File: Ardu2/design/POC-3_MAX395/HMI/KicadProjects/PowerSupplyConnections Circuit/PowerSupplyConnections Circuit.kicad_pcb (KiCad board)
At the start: 2 copper layers, 51.1 x 42.9 mm, 20 parts, among them P1 GND, P2 GND, P3 Wiper, P4 Wiper, P5 3.3v, P6 5v

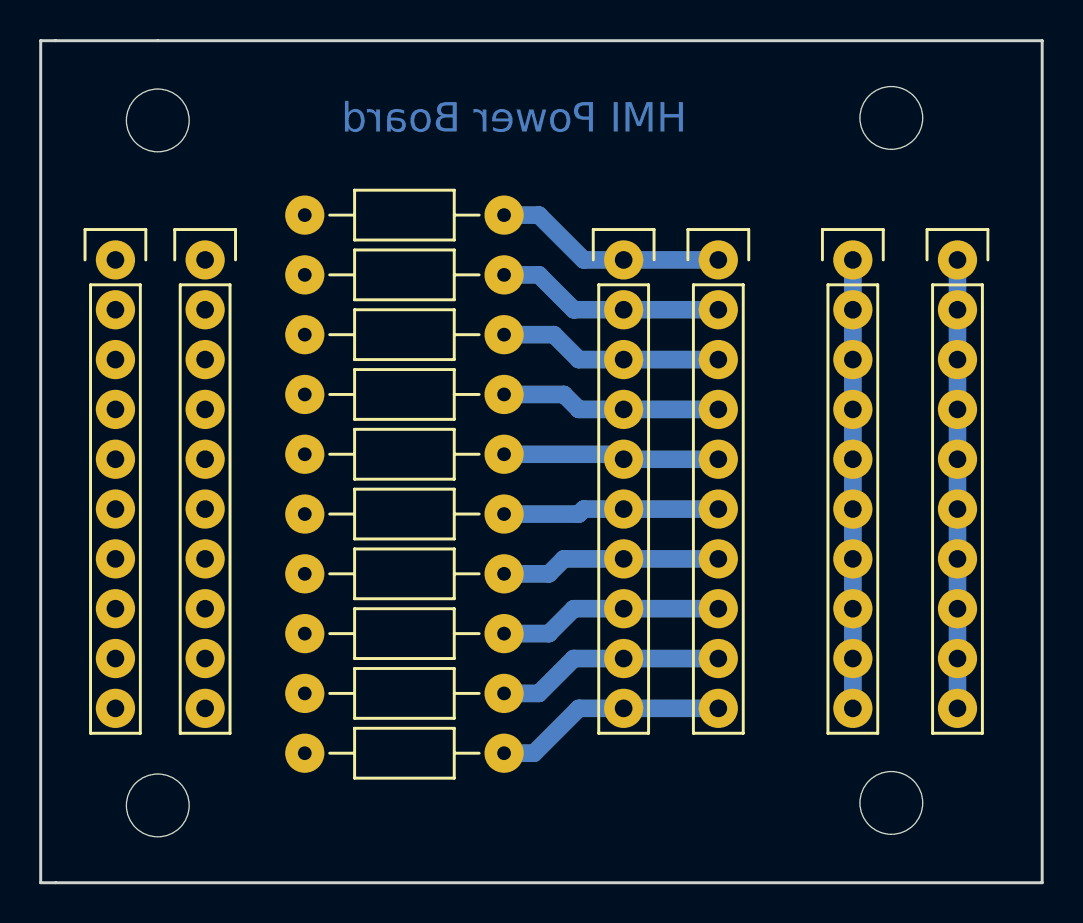
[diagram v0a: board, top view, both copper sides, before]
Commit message: final version pf power distribution board pcb
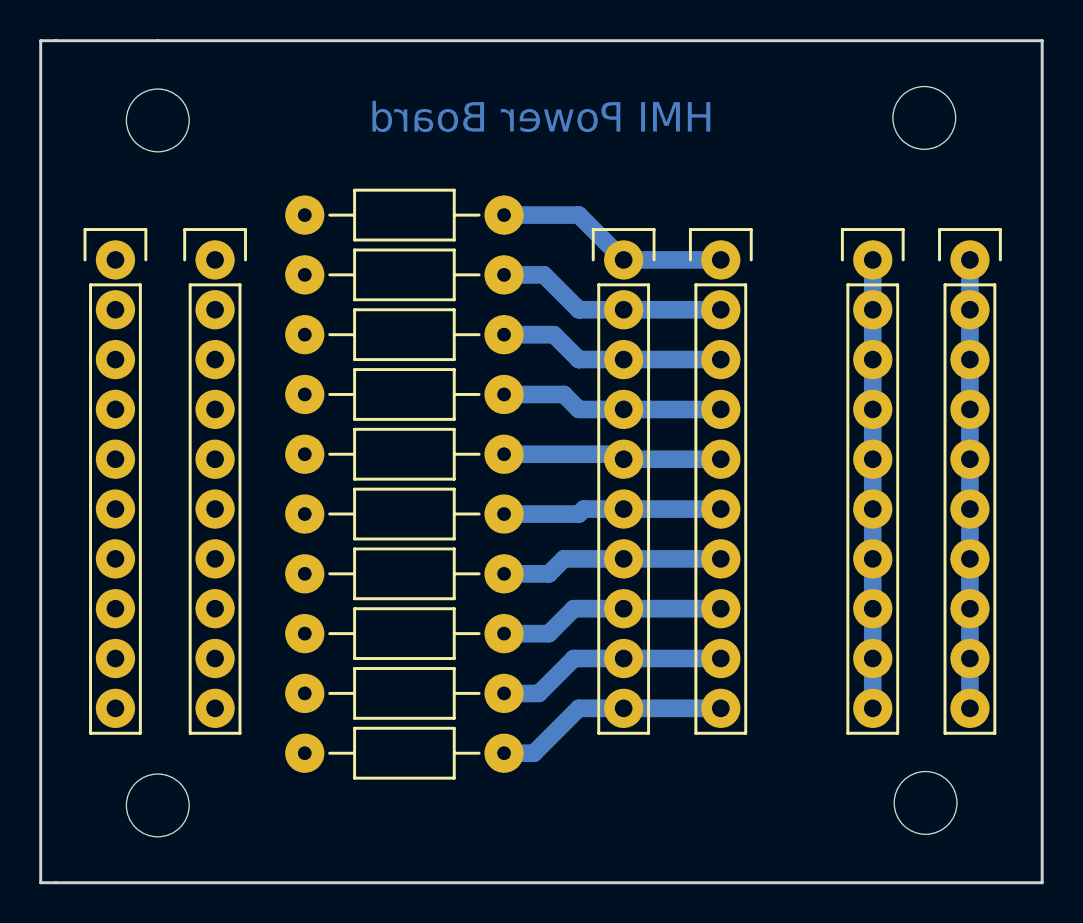
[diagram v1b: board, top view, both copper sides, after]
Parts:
- moved P6 1.02 mm to (165.9, 109.7)
- moved P5 0.63 mm to (170.8, 109.7)
- moved P2 0.51 mm to (132.3, 109.7)
- moved P3 0.13 mm to (158.1, 109.7)
